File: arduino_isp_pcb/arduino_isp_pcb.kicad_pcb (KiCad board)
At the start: 2 copper layers, 8 parts, among them J1 Conn_02x05_Odd_Even

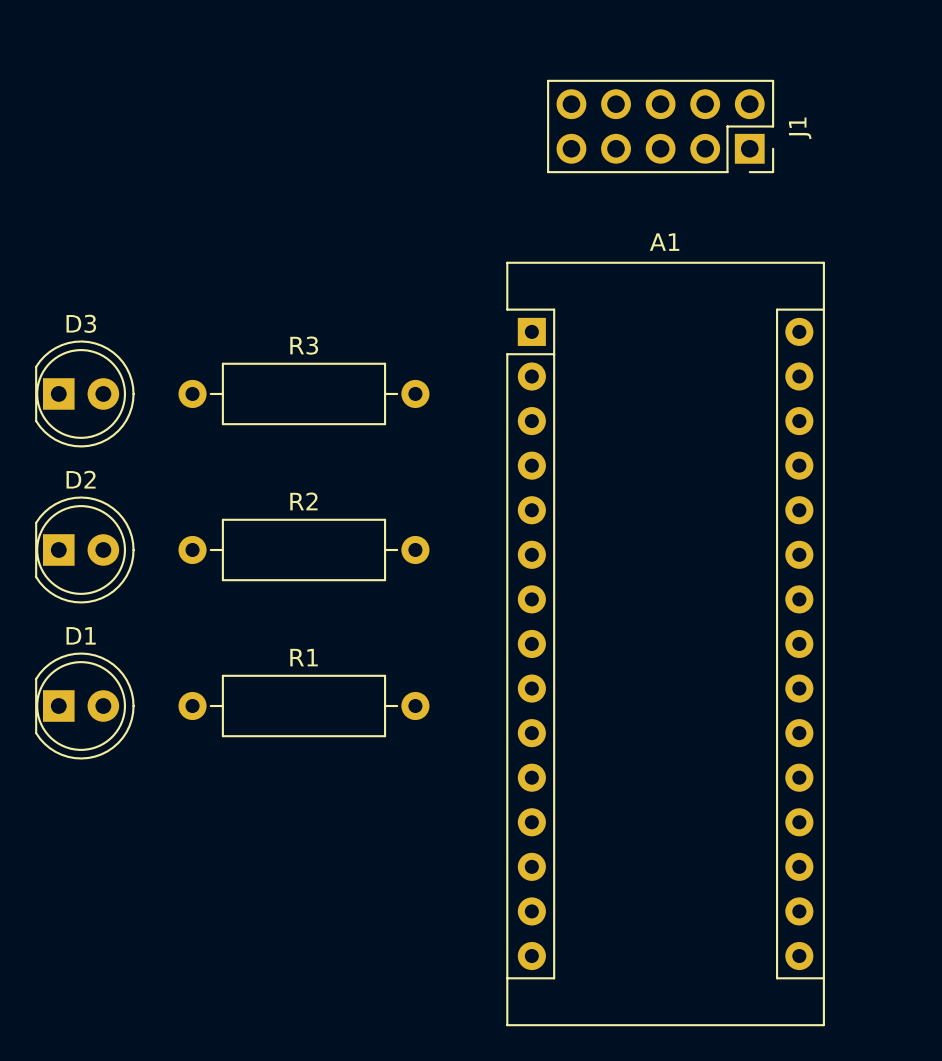
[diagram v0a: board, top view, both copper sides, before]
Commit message: PCB: add pcb
Route PCB
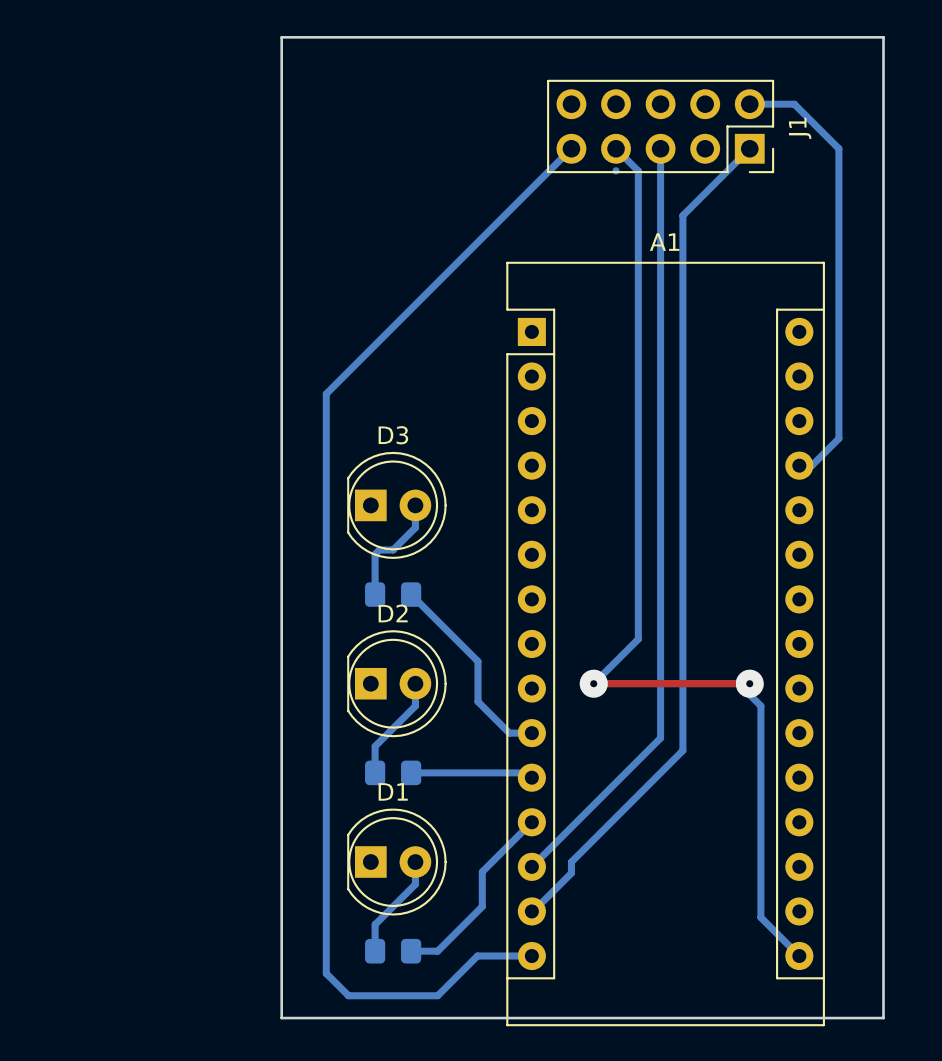
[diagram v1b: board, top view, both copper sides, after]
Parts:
- R1, R2, R3: footprint Resistor_THT:R_Axial_DIN0309_L9.0mm_D3.2mm_P12.70mm_Horizontal -> Resistor_SMD:R_0805_2012Metric_Pad1.15x1.40mm_HandSolder; moved to B.Cu
- moved D1 19.9 mm to (124.5, 137.2)
- moved D2 19.3 mm to (124.5, 127.0)
- moved D3 18.9 mm to (124.5, 116.8)
- moved R1 18.1 mm to (125.7, 142.2)
- moved R2 17.1 mm to (125.7, 132.1)
- moved R3 16.2 mm to (125.7, 121.9)
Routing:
- net MISO: track 0.00 -> 66.0 mm
- net SCLK: track 0.00 -> 57.6 mm, vias 0 -> 2
- net MOSI: track 0.00 -> 48.6 mm
- net T_RST: track 0.00 -> 44.0 mm
- net +5V: track 0.00 -> 25.5 mm
- net LED_PROG: track 0.00 -> 11.5 mm
- net LED_HB: track 0.00 -> 11.1 mm
- net LED_ERROR: track 0.00 -> 6.99 mm
- net Net-(D3-Pad2): track 0.00 -> 6.49 mm
- net Net-(D2-Pad2): track 0.00 -> 6.03 mm
- net Net-(D1-Pad2): track 0.00 -> 6.03 mm
- added copper zone on B.Cu, net GND
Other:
- board outline added: 34.3 x 55.9 mm

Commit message: PCB: add 6 pins AVR ISP connector
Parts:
- added J2: Conn_02x03_Odd_Even, Connector_PinHeader_2.54mm:PinHeader_2x03_P2.54mm_Vertical, F.Cu at (127.3, 101.0)
- J1: footprint Connector_PinSocket_2.54mm:PinSocket_2x05_P2.54mm_Vertical -> Connector_PinHeader_2.54mm:PinHeader_2x05_P2.54mm_Vertical
- moved J1 6.97 mm to (139.2, 97.8), turned to 90 degrees
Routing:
- net T_RST: track 44.0 -> 107.6 mm
- net GND: track 0.00 -> 61.6 mm, vias 0 -> 2
- net +5V: track 25.5 -> 63.9 mm, vias 0 -> 2
- net SCLK: track 57.6 -> 95.7 mm
- net MOSI: track 48.6 -> 74.0 mm
- net MISO: track 66.0 -> 82.6 mm, vias 0 -> 2
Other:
- board size 34.3 x 55.9 mm -> 35.6 x 55.9 mm
